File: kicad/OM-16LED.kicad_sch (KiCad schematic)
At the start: 99 parts, among them J1 2EDGVC-5.0-04P, J2 2EDGVC-5.0-06P, J3 2EDGVC-5.0-06P, J4 2EDGVC-5.0-06P, J5 2EDGVC-5.0-06P, J6 02x03 1.27, Q1 NTMFS4D0N08X, Q10 NTMFS4D0N08X, Q11 NTMFS4D0N08X, Q12 NTMFS4D0N08X, Q13 NTMFS4D0N08X, Q14 NTMFS4D0N08X, Q15 NTMFS4D0N08X, Q16 NTMFS4D0N08X, Q2 NTMFS4D0N08X, Q3 NTMFS4D0N08X, Q4 NTMFS4D0N08X, Q5 NTMFS4D0N08X, Q6 NTMFS4D0N08X, Q7 NTMFS4D0N08X, Q8 NTMFS4D0N08X, Q9 NTMFS4D0N08X, U1 STM32G474RETx, U10 R-78E12-1.0, U11 R-78E3.3-0.5, U12 THVD1450DR, U2 2EDN7534B, U3 2EDN7534B, U4 2EDN7534B, U5 2EDN7534B, U6 2EDN7534B, U7 2EDN7534B, U8 2EDN7534B, U9 2EDN7534B

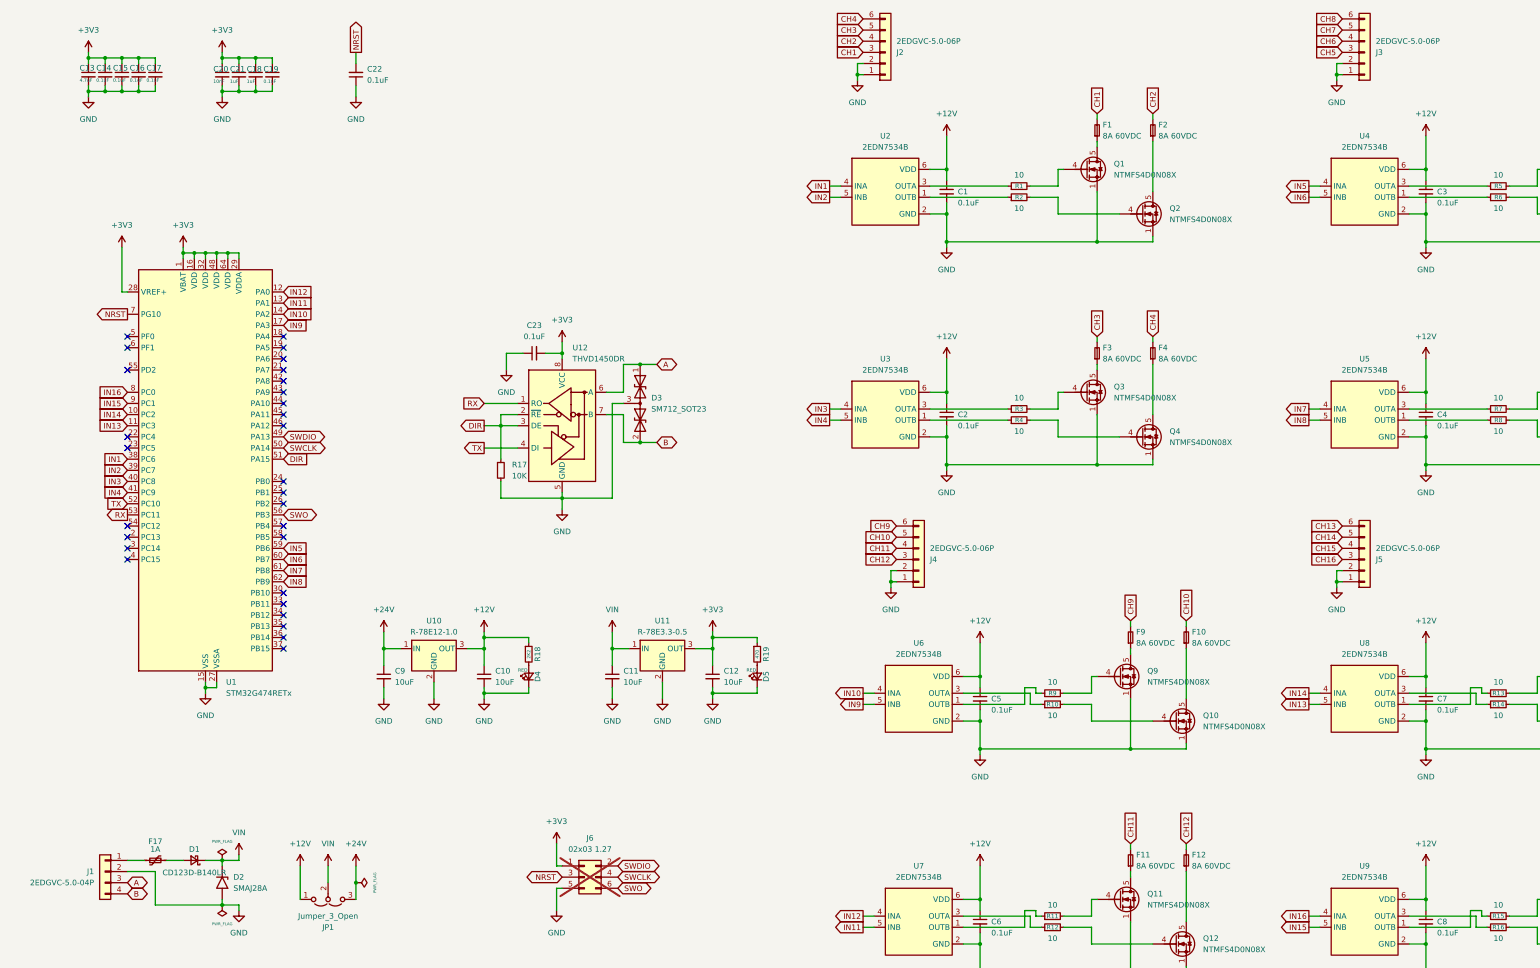
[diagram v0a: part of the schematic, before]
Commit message: feat: add screw terminals
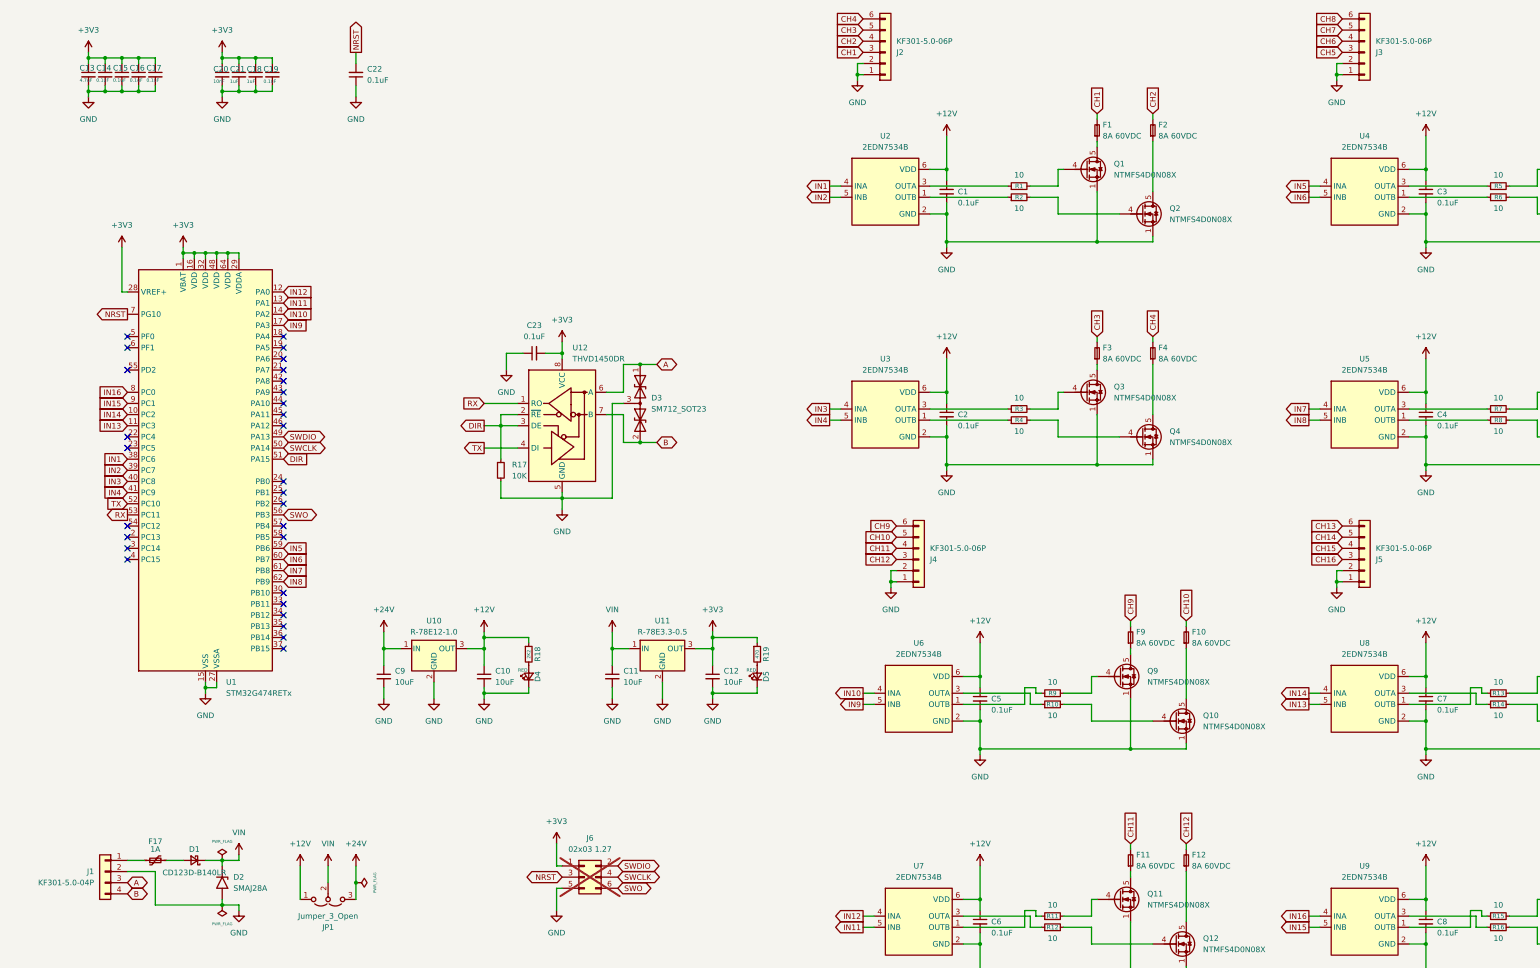
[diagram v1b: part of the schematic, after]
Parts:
- J1: value 2EDGVC-5.0-04P -> KF301-5.0-04P; footprint Library:TerminalBlock_DEGSON_2EDGVC-5.0-04P_No_SilkScreen -> Library:TerminalBlock_KF301-5.0-04P_No_SilkScreen; LCSC# C441377 -> (none); Manufacturer DEGSON -> KEFA; Part Number 10030002303 -> (none)
- J2, J3, J4, J5: value 2EDGVC-5.0-06P -> KF301-5.0-06P; footprint Library:TerminalBlock_DEGSON_2EDGVC-5.0-06P_No_SilkScreen -> Library:TerminalBlock_KF301-5.0-06P_No_SilkScreen; LCSC# C441379 -> (none); Manufacturer DEGSON -> KEFA; Part Number 10030002306 -> (none)
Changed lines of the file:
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@@
 			)
 		)
-		(property "Value" "2EDGVC-5.0-06P"
+		(property "Value" "KF301-5.0-06P"
 			(at 226.06 142.2401 0)
 			(effects
@@
 			)
 		)
-		(property "Footprint" "Library:TerminalBlock_DEGSON_2EDGVC-5.0-06P_No_SilkScreen"
+		(property "Footprint" "Library:TerminalBlock_KF301-5.0-06P_No_SilkScreen"
 			(at 223.52 144.78 0)
 			(effects
@@
 			)
 		)
-		(property "LCSC#" "C441379"
+		(property "LCSC#" ""
 			(at 223.52 144.78 0)
 			(effects
@@
 			)
 		)
-		(property "Manufacturer" "DEGSON"
+		(property "Manufacturer" "KEFA"
 			(at 223.52 144.78 0)
 			(effects
@@
 			)
 		)
-		(property "Part Number" "10030002306"
+		(property "Part Number" ""
 			(at 223.52 144.78 0)
 			(effects
@@
 			)
 		)
-		(property "Value" "2EDGVC-5.0-04P"
+		(property "Value" "KF301-5.0-04P"
 			(at 35.56 218.4399 0)
 			(effects
@@
 			)
 		)
-		(property "Footprint" "Library:TerminalBlock_DEGSON_2EDGVC-5.0-04P_No_SilkScreen"
+		(property "Footprint" "Library:TerminalBlock_KF301-5.0-04P_No_SilkScreen"
 			(at 38.1 215.9 0)
 			(effects
@@
 			)
 		)
-		(property "LCSC#" "C441377"
+		(property "LCSC#" ""
 			(at 38.1 215.9 0)
 			(effects
@@
 			)
 		)
-		(property "Manufacturer" "DEGSON"
+		(property "Manufacturer" "KEFA"
 			(at 38.1 215.9 0)
 			(effects
@@
 			)
 		)
-		(property "Part Number" "10030002303"
+		(property "Part Number" ""
 			(at 38.1 215.9 0)
 			(effects
@@
 			)
 		)
-		(property "Value" "2EDGVC-5.0-06P"
+		(property "Value" "KF301-5.0-06P"
 			(at 327.66 26.6701 0)
 			(effects
@@
 			)
 		)
-		(property "Footprint" "Library:TerminalBlock_DEGSON_2EDGVC-5.0-06P_No_SilkScreen"
+		(property "Footprint" "Library:TerminalBlock_KF301-5.0-06P_No_SilkScreen"
 			(at 325.12 29.21 0)
 			(effects
@@
 			)
 		)
-		(property "LCSC#" "C441379"
+		(property "LCSC#" ""
 			(at 325.12 29.21 0)
 			(effects
@@
 			)
 		)
-		(property "Manufacturer" "DEGSON"
+		(property "Manufacturer" "KEFA"
 			(at 325.12 29.21 0)
 			(effects
@@
 			)
 		)
-		(property "Part Number" "10030002306"
+		(property "Part Number" ""
 			(at 325.12 29.21 0)
 			(effects
@@
 			)
 		)
-		(property "Value" "2EDGVC-5.0-06P"
+		(property "Value" "KF301-5.0-06P"
 			(at 327.66 142.2401 0)
 			(effects
@@
 			)
 		)
-		(property "Footprint" "Library:TerminalBlock_DEGSON_2EDGVC-5.0-06P_No_SilkScreen"
+		(property "Footprint" "Library:TerminalBlock_KF301-5.0-06P_No_SilkScreen"
 			(at 325.12 144.78 0)
 			(effects
@@
 			)
 		)
-		(property "LCSC#" "C441379"
+		(property "LCSC#" ""
 			(at 325.12 144.78 0)
 			(effects
@@
 			)
 		)
-		(property "Manufacturer" "DEGSON"
+		(property "Manufacturer" "KEFA"
 			(at 325.12 144.78 0)
 			(effects
@@
 			)
 		)
-		(property "Part Number" "10030002306"
+		(property "Part Number" ""
 			(at 325.12 144.78 0)
 			(effects
@@
 			)
 		)
-		(property "Value" "2EDGVC-5.0-06P"
+		(property "Value" "KF301-5.0-06P"
 			(at 218.44 26.6701 0)
 			(effects
@@
 			)
 		)
-		(property "Footprint" "Library:TerminalBlock_DEGSON_2EDGVC-5.0-06P_No_SilkScreen"
+		(property "Footprint" "Library:TerminalBlock_KF301-5.0-06P_No_SilkScreen"
 			(at 215.9 29.21 0)
 			(effects
@@
 			)
 		)
-		(property "LCSC#" "C441379"
+		(property "LCSC#" ""
 			(at 215.9 29.21 0)
 			(effects
@@
 			)
 		)
-		(property "Manufacturer" "DEGSON"
+		(property "Manufacturer" "KEFA"
 			(at 215.9 29.21 0)
 			(effects
@@
 			)
 		)
-		(property "Part Number" "10030002306"
+		(property "Part Number" ""
 			(at 215.9 29.21 0)
 			(effects
